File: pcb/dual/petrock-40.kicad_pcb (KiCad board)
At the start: 2 copper layers, 242.5 x 87.9 mm, 102 parts, among them J1 MJ-4PP-9, J2 OLED, J3 MJ-4PP-9, J4 OLED, SW1 SW_PUSH, SW10 SW_PUSH, SW11 SW_PUSH, SW12 SW_PUSH, SW13 SW_PUSH, SW14 SW_PUSH, SW15 SW_PUSH, SW16 SW_PUSH, SW17 SW_PUSH, SW18 SW_PUSH, SW2 SW_PUSH, SW20 SW_PUSH, SW21 SW_PUSH, SW22 SW_PUSH, SW23 SW_PUSH, SW24 SW_PUSH, SW25 SW_PUSH, SW26 SW_PUSH, SW27 SW_PUSH, SW29 SW_PUSH, SW3 SW_PUSH, SW30 SW_PUSH, SW31 SW_PUSH, SW32 SW_PUSH, SW33 SW_PUSH, SW34 SW_PUSH, SW35 SW_PUSH, SW36 SW_PUSH, SW37 SW_PUSH, SW38 SW_PUSH, SW39 SW_PUSH, SW4 SW_PUSH, SW41 SW_PUSH, SW42 SW_PUSH, SW43 SW_PUSH, SW44 SW_PUSH, SW5 SW_PUSH, SW6 SW_PUSH, SW8 SW_PUSH, SW9 SW_PUSH, U1 ProMicro, U2 ProMicro

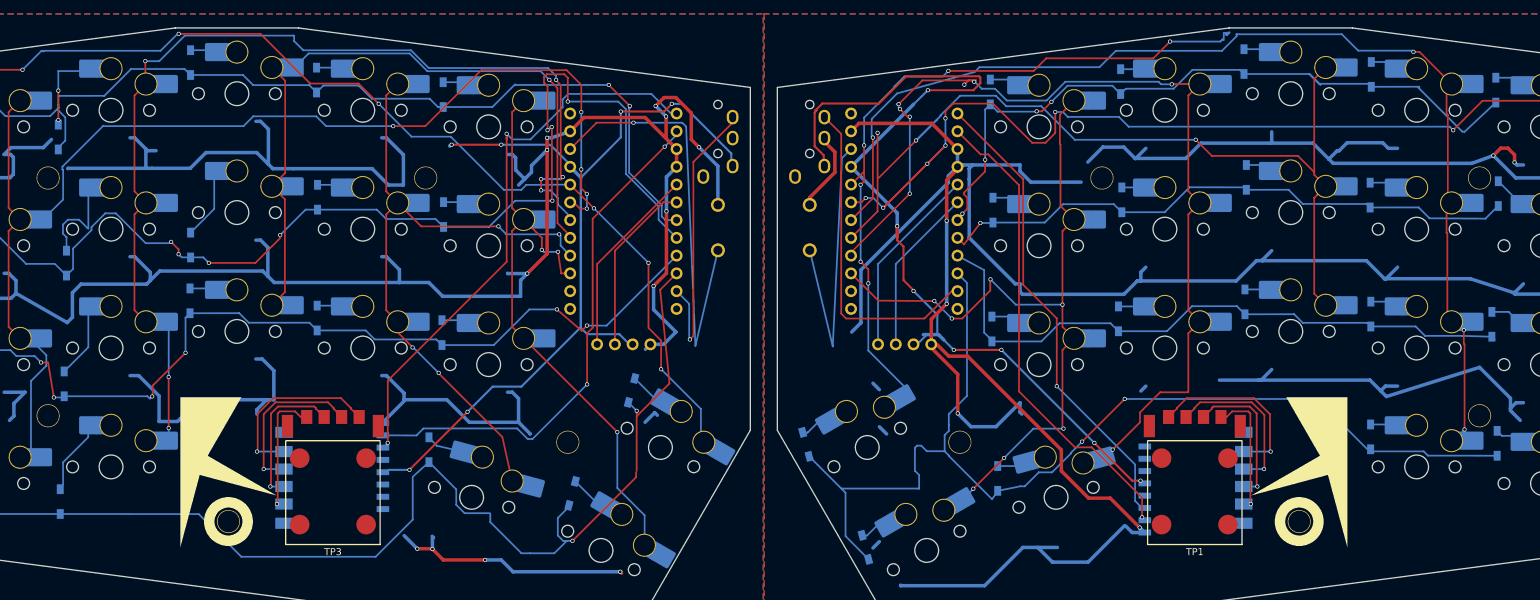
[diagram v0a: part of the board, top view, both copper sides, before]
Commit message: Standoffs in a rectangle, screw holes back in the switch plate
The standoff stack is holykeebs': a spacer through the main board's 3.1 mm
hole, a top screw through the switch plate, a bottom screw through the
bottom plate; the main board hangs from the switches. The plate's screw
holes, removed early on as supposed OLED-cover holes, are back (2.1 mm)
over every standoff.

Per half, four standoffs sit at four-key centres forming a 54 x 34 mm
rectangle (pinky|ring and index|inner index, top and bottom) and one at
the thumbs. The logo's standoff moves to the index bottom, so the logo
carries a solid 7 mm dot on board and plate. README: hardware (5 mm round
spacers; small-head top screws where four keys meet), assembly and feet.
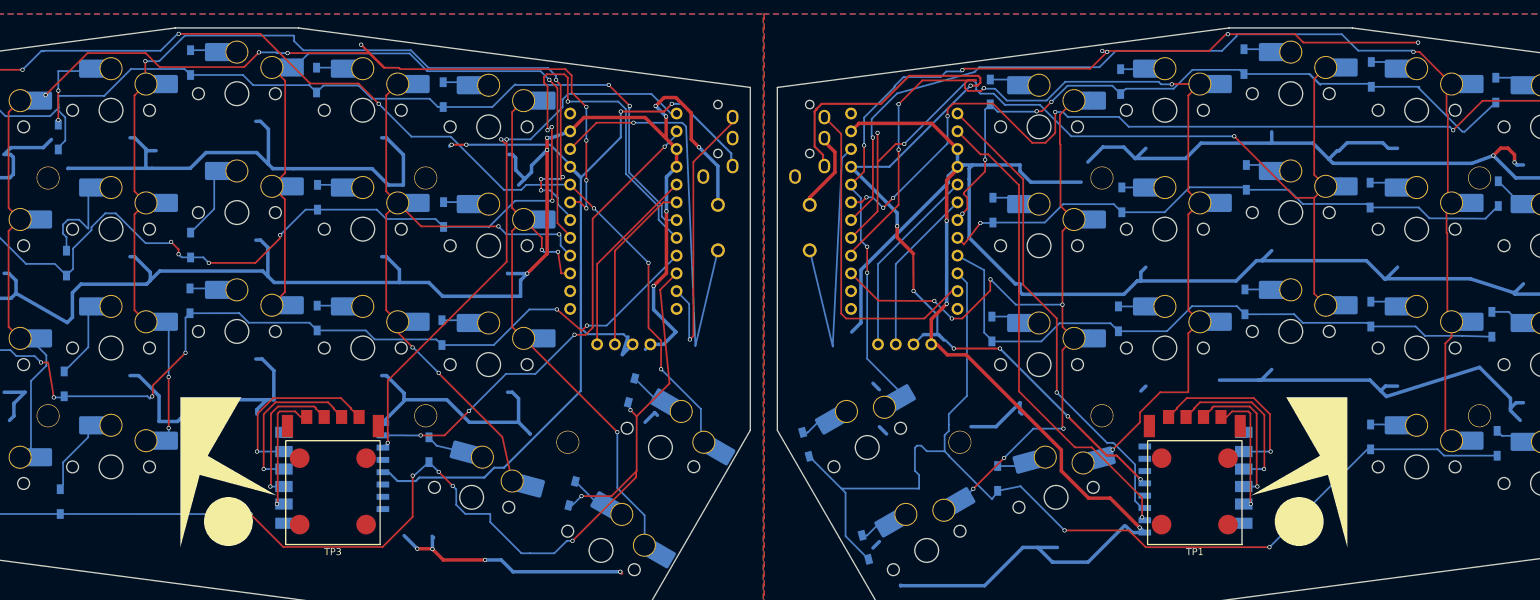
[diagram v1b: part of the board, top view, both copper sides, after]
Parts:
- moved h2 32.0 mm to (107.5, 107.2)
- moved h2 32.0 mm to (204.2, 107.2)
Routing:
- net col0_r: track 102.7 -> 129.4 mm, vias 6 -> 8
- net GNDA: track 495.6 -> 482.4 mm, vias 6 -> 5
- net col1_r: track 191.3 -> 178.9 mm, vias 7 -> 6
- net VCC: track 159.9 -> 149.2 mm, vias 6 -> 4
- net TP_DATA_L: track 74.2 -> 68.7 mm, vias 2 -> 4
- net row3: track 164.0 -> 167.5 mm, vias 2 -> 7
- net VDD: track 131.0 -> 128.3 mm
- net col1: track 165.4 -> 167.6 mm, vias 5 -> 8
- net col3_r: track 129.9 -> 128.4 mm
- net row3_r: track 157.3 -> 158.6 mm
- net TP_CLK: track 66.8 -> 67.3 mm
- net col4_r: track 138.8 -> 139.0 mm, vias 8 -> 5
- net col2_r: track 157.2 -> 157.3 mm, vias 4 -> 2
- net TP_CLK_L: track 81.1 -> 81.2 mm, vias 2 -> 3

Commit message: Jack pads masked tight, version stamp, A1-A4 for the trackpoint parts
The stock jack footprint's solder-mask openings showed bare ground beside
the supply pad, where a hand-soldered bridge would short it: the jack pads'
mask opening now matches the pad (no solder-mask bridges left; DRC has no
errors). holykeebs' revision stamp gives way to ours (name, version,
repository) on the back between the controller's pin rows. The trackpoint
sensor and controller boards become A1-A4 (assemblies), not TP (test point).
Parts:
- renumbered TP1 to A1, TP2 to A2, TP3 to A3, TP4 to A4
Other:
- board text added: "PETROCK-40 v3.10"
- board text added: "github.com/dycli/petrock"
- board text removed: "271364f"

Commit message: Boards, plates and renders built from 06b7685 (the hash printed on the boards)
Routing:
- net col1: track 167.6 -> 194.9 mm, vias 8 -> 10
- net VDD: track 128.3 -> 109.1 mm, vias 7 -> 8
- net col0_r: track 129.4 -> 135.5 mm, vias 8 -> 10
- net col2: track 149.1 -> 153.1 mm, vias 7 -> 5
- net col3_r: track 128.4 -> 126.0 mm, vias 3 -> 5
- net col0: track 150.7 -> 152.0 mm, vias 7 -> 10
- net col1_r: track 178.9 -> 177.6 mm, vias 6 -> 5
- net col4_r: track 139.0 -> 137.7 mm, vias 5 -> 6
- net row3_r: track 158.6 -> 157.4 mm
- net GNDA: track 482.4 -> 483.4 mm
- net row2: track 133.2 -> 133.7 mm, vias 6 -> 10
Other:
- board text added: "06b7685"
- board text removed: "PETROCK-40 v3.10"
- board text removed: "github.com/dycli/petrock"

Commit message: Boards, plates and renders built from b9e0fd4 (the hash printed on the boards)
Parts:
- moved D15 8.83 mm to (55.9, 93.9)
- moved D13 8.69 mm to (55.9, 110.9)
- moved D9 8.56 mm to (55.9, 76.9)
- moved D1 8.39 mm to (37.9, 113.2)
- moved D10 8.34 mm to (73.9, 74.5)
- moved D3 7.59 mm to (55.9, 59.9)
- moved D14 5.29 mm to (37.9, 96.2)
- moved D29 3.76 mm to (260.6, 79.2)
- moved D35 2.16 mm to (260.6, 96.2)
- moved D22 2.04 mm to (260.6, 113.2)
- moved D21 1.67 mm to (128.7, 120.0), turned to 60 degrees
- moved D45 1.67 mm to (137.2, 105.3), turned to 60 degrees
- moved D20 1.67 mm to (108.6, 113.6), turned to 75 degrees
- moved D23 1.55 mm to (260.6, 62.2)
- moved D2 1.51 mm to (37.9, 62.2)
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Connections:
- SW20 pad 1: col4 -> col3
- SW21 pad 1: col5 -> col4
- SW41 pad 1: col4_r -> col3_r
- SW42 pad 1: col5_r -> col4_r
- SW43 pad 1: col0 -> col5
- SW44 pad 1: col0_r -> col5_r
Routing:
- net GNDA: track 483.4 -> 4.31 mm, vias 5 -> 107
- net GND: track 448.7 -> 4.64 mm, vias 12 -> 118
- net col0: track 152.0 -> 0.00 mm, vias 10 -> 0
- net col0_r: track 135.5 -> 0.00 mm, vias 10 -> 0
- net VDD: track 109.1 -> 201.0 mm, vias 8 -> 1
- net col3_r: track 126.0 -> 209.7 mm, vias 5 -> 2
- net col3: track 98.9 -> 172.8 mm, vias 1 -> 2
- net TP_DATA: track 68.2 -> 127.7 mm
- net VCC: track 149.2 -> 208.3 mm, vias 4 -> 2
- net TP_DATA_L: track 68.7 -> 126.7 mm, vias 4 -> 1
- net TP_CLK: track 67.3 -> 124.7 mm
- net TP_CLK_L: track 81.2 -> 129.7 mm, vias 3 -> 1
- net col1: track 194.9 -> 147.2 mm, vias 10 -> 2
- net col4: track 94.2 -> 123.4 mm, vias 4 -> 2
- net col2: track 153.1 -> 125.0 mm, vias 5 -> 2
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- added copper zone on F.Cu, net GND
- added copper zone on F.Cu, net GNDA
- removed copper zone on F.Cu, net (none)
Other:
- board text added: "b9e0fd4"
- board text removed: "06b7685"

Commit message: Boards, plates and renders built from 86592b8 (the hash printed on the boards); adds the Petrock-42
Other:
- board text added: "86592b8"
- board text removed: "b9e0fd4"
